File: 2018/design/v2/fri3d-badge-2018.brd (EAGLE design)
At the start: 80 x 60 mm, 134 parts

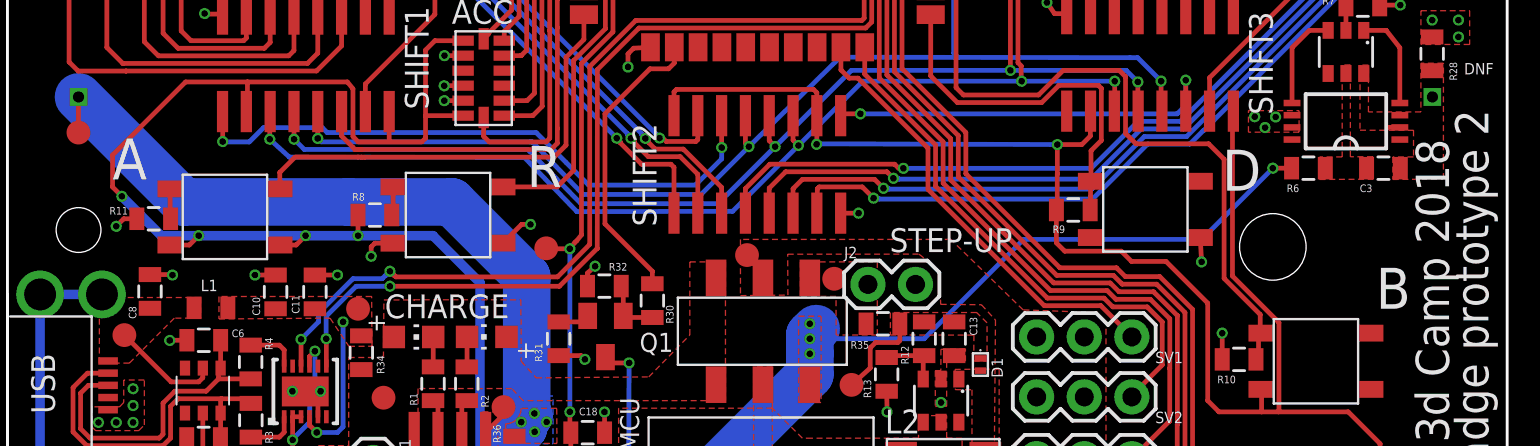
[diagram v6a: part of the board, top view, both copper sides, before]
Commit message: "fixed" incorrect labels ;-)
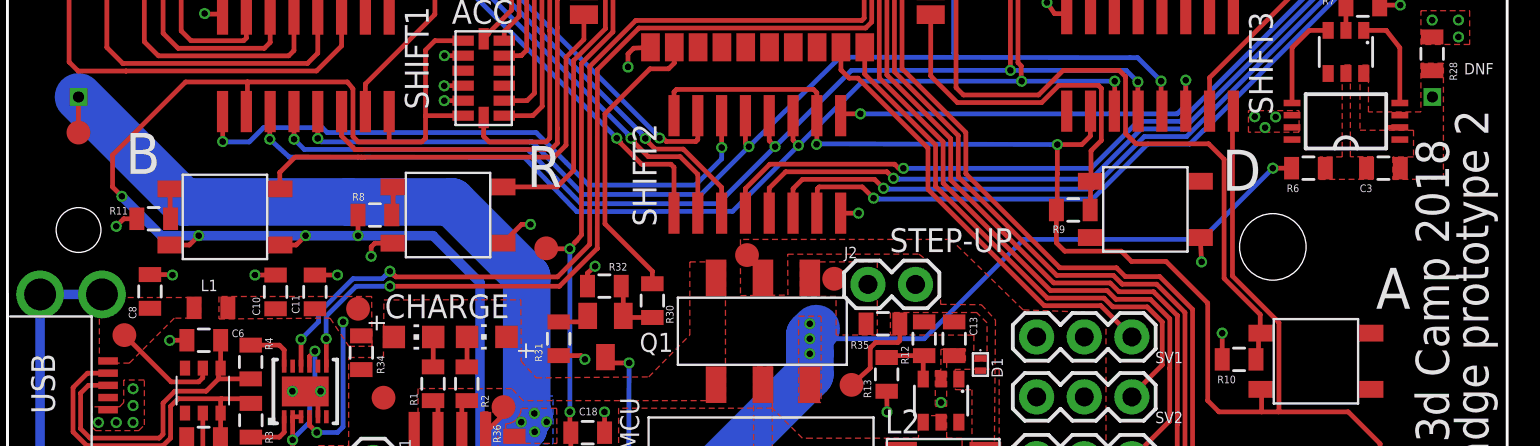
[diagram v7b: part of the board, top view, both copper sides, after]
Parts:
- moved A 58.7 mm to (69.8, 16.0)
- moved B 58.7 mm to (11.6, 23.7)
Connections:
- net BUTTON-A: now also A.1, A.2; no longer B.1, B.2
- net BUTTON-B: now also B.1, B.2; no longer A.1, A.2
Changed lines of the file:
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@@
 <attribute name="NAME" x="64.8" y="25.1" size="2.1844" layer="25"/>
 </element>
-<element name="B" library="switches" package="SWITCH-MOMENTARY-4.5MM" value="SWITCH-MOMENTARY-4.5MM" x="69.8" y="16" smashed="yes">
+<element name="A" library="switches" package="SWITCH-MOMENTARY-4.5MM" value="SWITCH-MOMENTARY-4.5MM" x="69.8" y="16" smashed="yes">
 <attribute name="NAME" x="73" y="18.8" size="2.1844" layer="25"/>
 </element>
-<element name="A" library="switches" package="SWITCH-MOMENTARY-4.5MM" value="SWITCH-MOMENTARY-4.5MM" x="11.6" y="23.7" smashed="yes">
-<attribute name="NAME" x="5.6" y="25.7" size="2.1844" layer="25"/>
+<element name="B" library="switches" package="SWITCH-MOMENTARY-4.5MM" value="SWITCH-MOMENTARY-4.5MM" x="11.6" y="23.7" smashed="yes">
+<attribute name="NAME" x="6.3" y="26" size="2.1844" layer="25"/>
 </element>
 <element name="R8" library="passive" package="0805" value="10K" x="19.6" y="23.8" smashed="yes" rot="R180">
@@
 <contactref element="R8" pad="2"/>
 <contactref element="R9" pad="2"/>
+<contactref element="A" pad="4" route="any" routetag="G$1.2"/>
+<contactref element="A" pad="3" route="any" routetag="G$1.2"/>
 <contactref element="B" pad="4" route="any" routetag="G$1.2"/>
 <contactref element="B" pad="3" route="any" routetag="G$1.2"/>
-<contactref element="A" pad="4" route="any" routetag="G$1.2"/>
-<contactref element="A" pad="3" route="any" routetag="G$1.2"/>
 <contactref element="SHIFT1" pad="16"/>
 <contactref element="SHIFT1" pad="10"/>
@@
 </signal>
 <signal name="BUTTON-A">
-<contactref element="B" pad="1" route="any" routetag="G$1.1"/>
-<contactref element="B" pad="2" route="any" routetag="G$1.1"/>
+<contactref element="A" pad="1" route="any" routetag="G$1.1"/>
+<contactref element="A" pad="2" route="any" routetag="G$1.1"/>
 <contactref element="R10" pad="2"/>
 <wire x1="66.875" y1="17.5" x2="66.7375" y2="17.6375" width="0.254" layer="1"/>
@@
 </signal>
 <signal name="BUTTON-B">
-<contactref element="A" pad="1" route="any" routetag="G$1.1"/>
-<contactref element="A" pad="2" route="any" routetag="G$1.1"/>
+<contactref element="B" pad="1" route="any" routetag="G$1.1"/>
+<contactref element="B" pad="2" route="any" routetag="G$1.1"/>
 <contactref element="R11" pad="2"/>
 <contactref element="MCU" pad="14"/>
